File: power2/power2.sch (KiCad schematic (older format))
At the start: 40 parts, among them P1 CN3 from HL, P2 CONN_01X02, P3 CONN_01X03, P4 CONN_02X06, P5 CONN_01X02, P6 CONN_01X08, U1 ADC78H90CIMT, U2 Oki 5V Reg, U3 Oki 3.3V Reg, U4 LMC6482A

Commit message: v2rx changes and update to new kicad
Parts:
- C1: symbol CP1 -> CP1-RESCUE-power2
- C10, C11, C2, C3, C4, C9: symbol C -> C-RESCUE-power2
- D1, D2: footprint Diodes_SMD:SOD-123 -> (none)
- D3: value BZX84C 3V3 -> BZXB4C 3v3; footprint Diodes_SMD:SOD-123 -> (none)
- R1, R10, R2, R3, R4, R5, R6, R7, R8, R9: symbol R -> R-RESCUE-power2
- U4: symbol OP275 -> OP275-RESCUE-power2
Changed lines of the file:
@@
 EESchema Schematic File Version 2
+LIBS:power2-rescue
 LIBS:power
 LIBS:device
@@
 LIBS:memory
 LIBS:xilinx
-LIBS:special
 LIBS:microcontrollers
 LIBS:dsp
@@
 	4650 1100 5150 1100
 $Comp
-L GND #PWR01
+L GND-RESCUE-power2 #PWR01
 U 1 1 54BE578A
 P 6250 1500
@@
 $EndComp
 $Comp
-L GND #PWR02
+L GND-RESCUE-power2 #PWR02
 U 1 1 54B9B387
 P 5150 1500
@@
 	4650 1200 4750 1200
 $Comp
-L GND #PWR03
+L GND-RESCUE-power2 #PWR03
 U 1 1 54B935E9
 P 4750 1500
@@
 $EndComp
 $Comp
-L CP1 C1
+L CP1-RESCUE-power2 C1
 U 1 1 54B82D65
 P 5150 1300
@@
 $EndComp
 $Comp
-L C C2
+L C-RESCUE-power2 C2
 U 1 1 551AAA77
 P 6250 1300
@@
 	10300 1100 10300 1800
 $Comp
-L GND #PWR04
+L GND-RESCUE-power2 #PWR04
 U 1 1 551AB7A4
 P 10300 1800
@@
 Connection ~ 10300 1200
 $Comp
-L GND #PWR05
+L GND-RESCUE-power2 #PWR05
 U 1 1 551ABA3D
 P 6900 1400
@@
 $EndComp
 $Comp
-L GND #PWR06
+L GND-RESCUE-power2 #PWR06
 U 1 1 551ABA65
 P 7800 1900
@@
 	8600 1600 8800 1600
 $Comp
-L GND #PWR07
+L GND-RESCUE-power2 #PWR07
 U 1 1 551AC024
 P 8450 1700
@@
 $EndComp
 $Comp
-L GND #PWR08
+L GND-RESCUE-power2 #PWR08
 U 1 1 551AC04B
 P 8500 1200
@@
 	9500 2600 9500 2750
 $Comp
-L GND #PWR09
+L GND-RESCUE-power2 #PWR09
 U 1 1 551AC911
 P 9500 2750
@@
 	9000 2500 9600 2500
 $Comp
-L GND #PWR010
+L GND-RESCUE-power2 #PWR010
 U 1 1 551ACBE1
 P 7950 2500
@@
 $EndComp
 $Comp
-L GND #PWR011
+L GND-RESCUE-power2 #PWR011
 U 1 1 551ACBFA
 P 8450 2800
@@
 	7600 3000 7600 3500
 $Comp
-L GND #PWR012
+L GND-RESCUE-power2 #PWR012
 U 1 1 551ACC6B
 P 7600 3500
@@
 	7200 3750 6350 3750
 $Comp
-L C C4
+L C-RESCUE-power2 C4
 U 1 1 551ACF21
 P 7000 3950
@@
 $EndComp
 $Comp
-L C C3
+L C-RESCUE-power2 C3
 U 1 1 551ACFBF
 P 6600 3950
@@
 $EndComp
 $Comp
-L GND #PWR013
+L GND-RESCUE-power2 #PWR013
 U 1 1 551AD095
 P 7000 4150
@@
 $EndComp
 $Comp
-L GND #PWR014
+L GND-RESCUE-power2 #PWR014
 U 1 1 551AD0B1
 P 6600 4150
@@
 	6000 3300 6000 3500
 $Comp
-L GND #PWR015
+L GND-RESCUE-power2 #PWR015
 U 1 1 551AD402
 P 6000 3500
@@
 Connection ~ 7600 3500
 $Comp
-L OP275 U4
+L OP275-RESCUE-power2 U4
 U 1 1 552BFD56
 P 6600 5000
@@
 $EndComp
 $Comp
-L OP275 U4
+L OP275-RESCUE-power2 U4
 U 2 1 552BFF04
 P 8100 5100
@@
 $EndComp
 $Comp
-L R R7
+L R-RESCUE-power2 R7
 U 1 1 552C03C4
 P 7800 5950
@@
 $EndComp
 $Comp
-L R R5
+L R-RESCUE-power2 R5
 U 1 1 552C077F
 P 7300 5000
@@
 $EndComp
 $Comp
-L R R6
+L R-RESCUE-power2 R6
 U 1 1 552C08A2
 P 7550 5450
@@
 $EndComp
 $Comp
-L R R8
+L R-RESCUE-power2 R8
 U 1 1 552C0983
 P 8450 5950
@@
 $EndComp
 $Comp
-L R R4
+L R-RESCUE-power2 R4
 U 1 1 552C09E6
 P 6200 5950
@@
 $EndComp
 $Comp
-L R R3
+L R-RESCUE-power2 R3
 U 1 1 552C0A88
 P 5900 5450
@@
 	5900 4900 5900 5200
 $Comp
-L GND #PWR016
+L GND-RESCUE-power2 #PWR016
 U 1 1 552C11D9
 P 6500 5300
@@
 	1    0    0    -1
 $EndComp
-$Comp
-L ZENER D2
-U 1 1 552C183F
-P 6650 5950
-F 0 "D2" H 6650 6050 50  0000 C CNN
-F 1 "1n5711" H 6650 5850 40  0000 C CNN
-F 2 "Diodes_SMD:SOD-123" H 6650 5950 60  0001 C CNN
-F 3 "" H 6650 5950 60  0000 C CNN
-	1    6650 5950
-	-1   0    0    1
-$EndComp
 Wire Wire Line
 	6950 5000 6950 5950
@@
 	6950 5950 6850 5950
 $Comp
-L GND #PWR017
+L GND-RESCUE-power2 #PWR017
 U 1 1 552C18EE
 P 5900 6050
@@
 $EndComp
 $Comp
-L GND #PWR018
+L GND-RESCUE-power2 #PWR018
 U 1 1 552C1913
 P 7550 6050
@@
 Connection ~ 5900 4900
 $Comp
-L R R2
+L R-RESCUE-power2 R2
 U 1 1 552C3533
 P 5500 5150
@@
 $EndComp
 $Comp
-L R R1
+L R-RESCUE-power2 R1
 U 1 1 552C36C8
 P 5500 4650
@@
 $EndComp
 $Comp
-L GND #PWR019
+L GND-RESCUE-power2 #PWR019
 U 1 1 552C39B6
 P 5500 5400
@@
 $EndComp
 $Comp
-L GND #PWR020
+L GND-RESCUE-power2 #PWR020
 U 1 1 552C3A08
 P 4650 4600
@@
 F 3 "" H 4650 4600 50  0000 C CNN
 	1    4650 4600
-	1    0    0    -1
-$EndComp
-$Comp
-L ZENER D1
-U 1 1 552C3BD5
-P 5700 4900
-F 0 "D1" H 5700 5000 50  0000 C CNN
-F 1 "1n5711" H 5700 4800 40  0000 C CNN
-F 2 "Diodes_SMD:SOD-123" H 5700 4900 60  0001 C CNN
-F 3 "" H 5700 4900 60  0000 C CNN
-	1    5700 4900
 	1    0    0    -1
 $EndComp
@@
 	4650 4500 4650 4600
 $Comp
-L C C9
+L C-RESCUE-power2 C9
 U 1 1 5530FFE1
 P 6100 5450
@@
 nADCCS
 $Comp
-L C C10
+L C-RESCUE-power2 C10
 U 1 1 5554C716
 P 5000 4400
@@
 Wire Wire Line
 	5200 4400 5500 4400
-$Comp
-L ZENER D3
-U 1 1 5558A709
-P 9000 3650
-F 0 "D3" H 9000 3750 50  0000 C CNN
-F 1 "BZX84C 3V3" H 9000 3550 40  0000 C CNN
-F 2 "Diodes_SMD:SOD-123" H 9000 3650 60  0001 C CNN
-F 3 "" H 9000 3650 60  0000 C CNN
-	1    9000 3650
-	0    -1   -1   0
-$EndComp
 Wire Wire Line
 	7850 2800 7850 4600
@@
 	8800 5100 8800 5950
 $Comp
-L R R10
+L R-RESCUE-power2 R10
 U 1 1 5558AFB4
 P 8700 3700
@@
 $EndComp
 $Comp
-L C C11
+L C-RESCUE-power2 C11
 U 1 1 5558B07B
 P 8400 3650
@@
 Connection ~ 6500 1600
 $Comp
-L R R9
+L R-RESCUE-power2 R9
 U 1 1 5558B562
 P 8700 3200
@@
 	8700 3950 8700 4050
 $Comp
-L GND #PWR021
+L GND-RESCUE-power2 #PWR021
 U 1 1 5558BF22
 P 8700 4050
@@
 	1300 2250 1300 2300
 $Comp
-L GND #PWR022
+L GND-RESCUE-power2 #PWR022
 U 1 1 558C247A
 P 1300 2300
@@
 $EndComp
 $Comp
-L GND #PWR023
+L GND-RESCUE-power2 #PWR023
 U 1 1 558FEEE6
 P 1850 2600
@@
 $EndComp
 $Comp
-L GND #PWR024
+L GND-RESCUE-power2 #PWR024
 U 1 1 558FEF19
 P 2450 2900
@@
 $EndComp
 $Comp
-L GND #PWR025
+L GND-RESCUE-power2 #PWR025
 U 1 1 558FEF4C
 P 2450 3300
@@
 $EndComp
 $Comp
-L GND #PWR026
+L GND-RESCUE-power2 #PWR026
 U 1 1 558FF17C
 P 1850 3000
@@
 Wire Wire Line
 	4700 2900 4600 2900
+$Comp
+L ZENER D1
+U 1 1 5675BF74
+P 5700 4900
+F 0 "D1" H 5700 5000 50  0000 C CNN
+F 1 "1n5711" H 5700 4800 50  0000 C CNN
+F 2 "" H 5700 4900 50  0001 C CNN
+F 3 "" H 5700 4900 50  0000 C CNN
+	1    5700 4900
+	-1   0    0    1
+$EndComp
+$Comp
+L ZENER D2
+U 1 1 5675C3B1
+P 6650 5950
+F 0 "D2" H 6650 6050 50  0000 C CNN
+F 1 "1n5711" H 6650 5850 50  0000 C CNN
+F 2 "" H 6650 5950 50  0001 C CNN
+F 3 "" H 6650 5950 50  0000 C CNN
+	1    6650 5950
+	1    0    0    -1
+$EndComp
+$Comp
+L ZENER D3
+U 1 1 5675DDD3
+P 9000 3650
+F 0 "D3" H 9000 3750 50  0000 C CNN
+F 1 "BZXB4C 3v3" H 9050 3550 50  0000 C CNN
+F 2 "" H 9000 3650 50  0001 C CNN
+F 3 "" H 9000 3650 50  0000 C CNN
+	1    9000 3650
+	0    1    1    0
+$EndComp
 $EndSCHEMATC

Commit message: Latest Rx updates
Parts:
- removed C12, C13, C14, C15: NFM21PC224R1C3D, SMDCAP:cfeed_0805, symbol Cap_FeedThrough
- removed P6: CONN_01X08, Pin_Headers:Pin_Header_Straight_1x08, symbol CONN_01X08
- added P6: CONN_01X05, symbol CONN_01X05
- added R11: 1k, Resistors_SMD:R_0805_HandSoldering, symbol R-RESCUE-power2
- added R12: 270, Resistors_SMD:R_0805_HandSoldering, symbol R-RESCUE-power2
- added R13, R14: 10k, Resistors_SMD:R_0805_HandSoldering, symbol R-RESCUE-power2
- added U5: LTV-847, DIP-16, symbol LTV-847
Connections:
- net GND: now also P6.1 (P1), P6.5 (P5), U5.11, U5.13, U5.15, U5.4, U5.9
- net at C2.1, L1.2, R9.1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: now also R11.1
- net at C6.2, L2.1, P4.5 (P5)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: now also R13.1, R14.1
- net at P1.10 (P10): now also R13.2, U5.16
- net at P1.6 (P6): now also R14.2, U5.12
- net at P1.8 (P8): now also R12.1
- new net: R11.2, U5.1, U5.5
- new net: R12.2, U5.3
- new net: P6.3 (P3), U5.14
- new net: P6.2 (P2), U5.2
- new net: P6.4 (P4), U5.6
- no-connect marks 3 -> 10
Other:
- note added: "CW in"
- note added: "CW out"
- note added: "P39 CN1 (3)"
- note added: "P41 CN1 (5)"
- note added: "P45 CN1 (7)"
- note added: "PTT in"
- note removed: "P39 CN1"
- note removed: "P41 CN1"
- note removed: "P45 CN1"

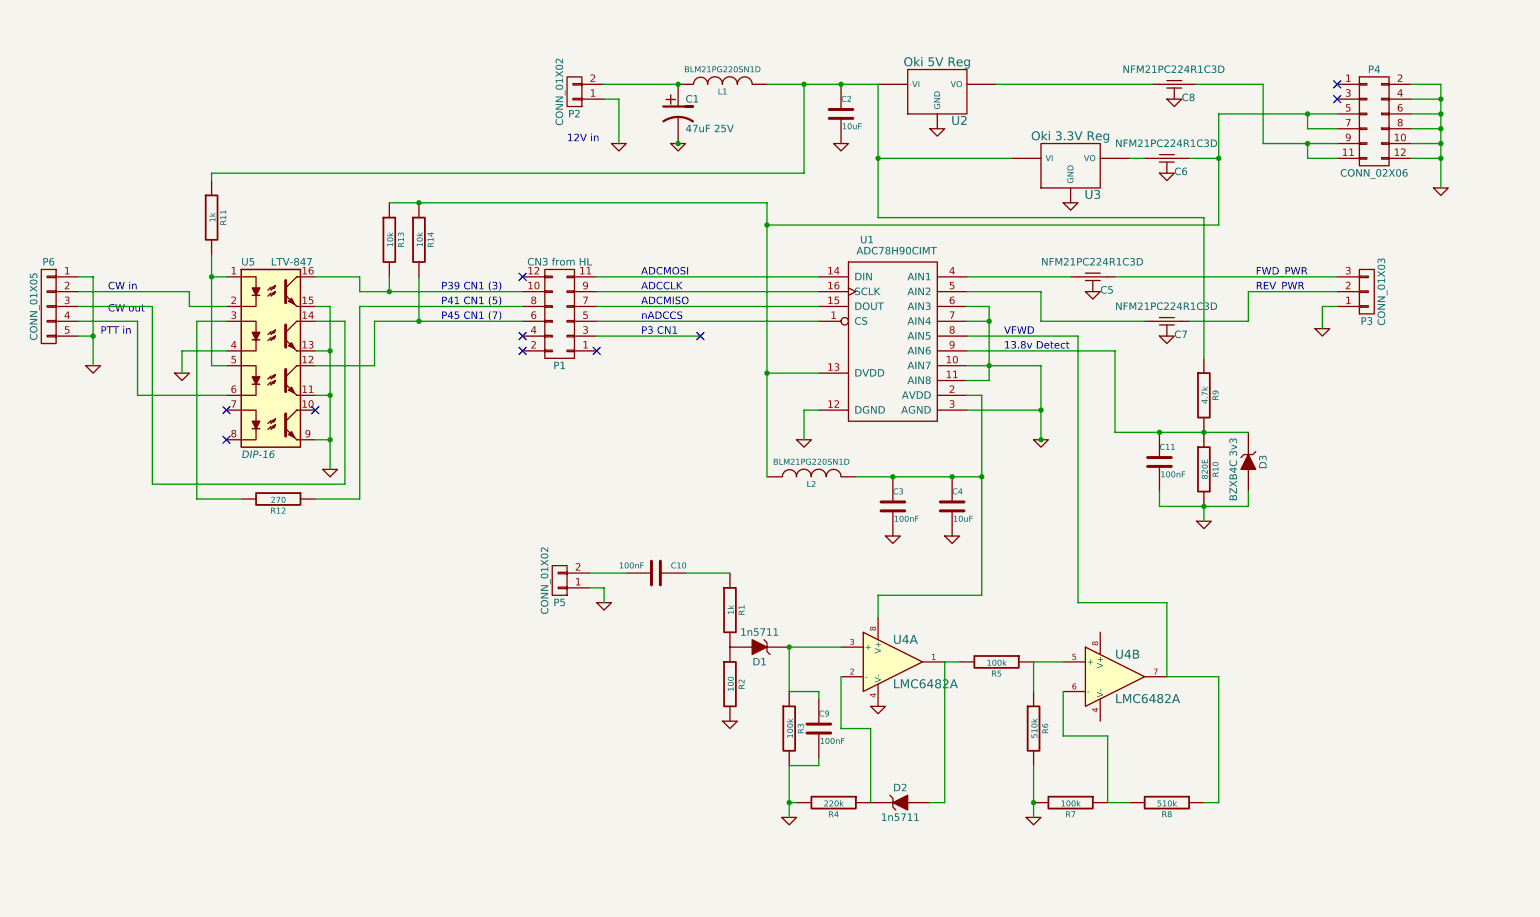
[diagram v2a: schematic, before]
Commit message: Updates for v1.1 amp and V1.4 ADC
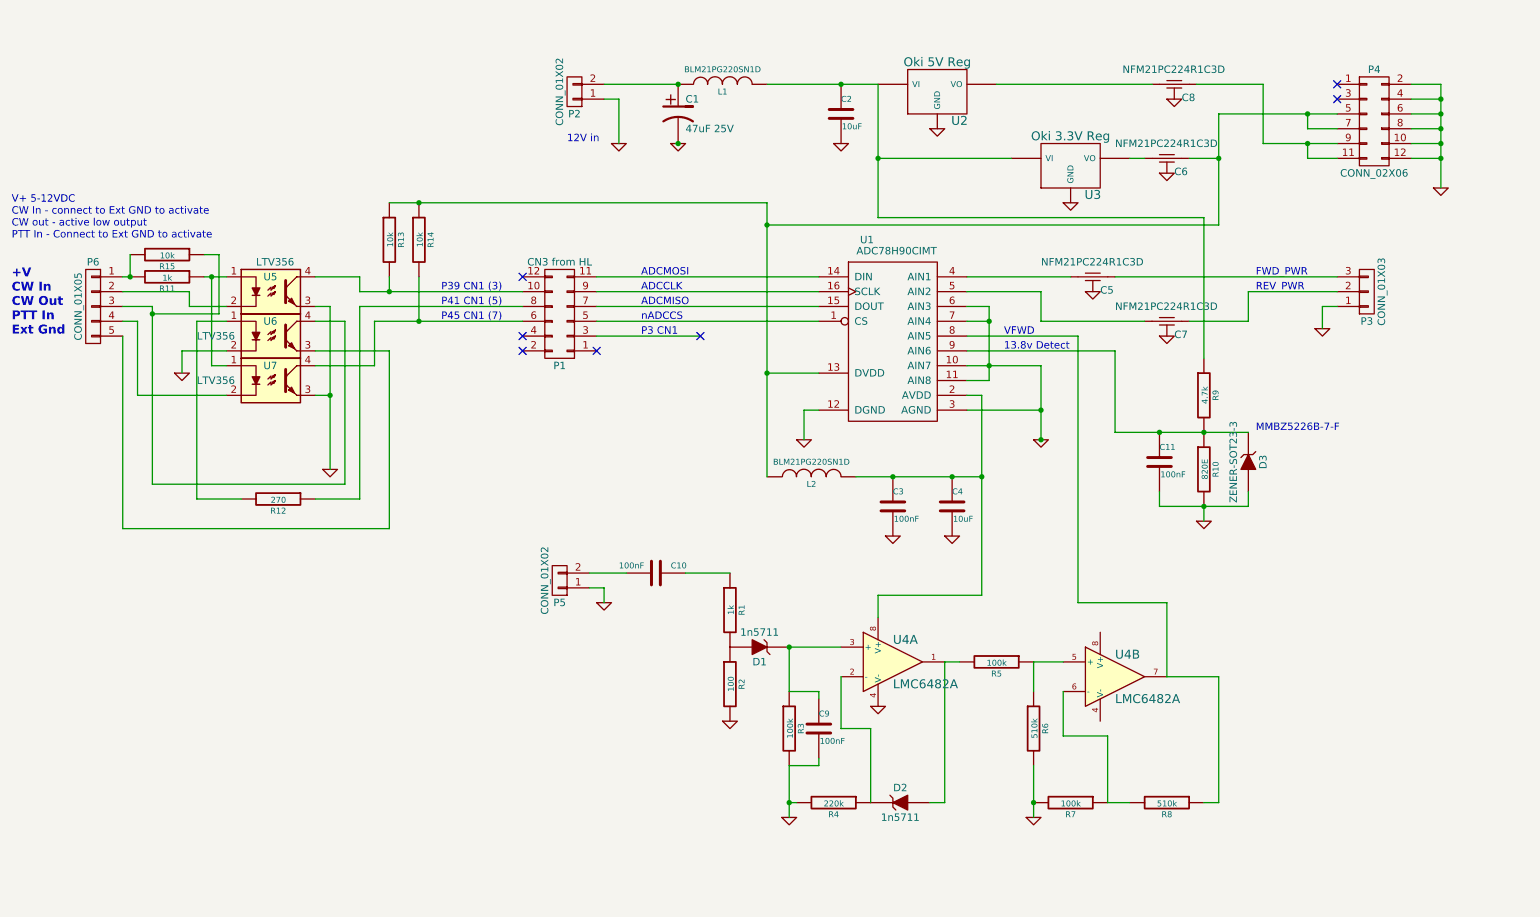
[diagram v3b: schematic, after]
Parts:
- removed D3: BZXB4C 3v3, symbol ZENER
- removed U5: LTV-847, DIP-16, symbol LTV-847
- added D3: ZENER-SOT23-3, symbol ZENER-SOT23-3
- added R15: 10k, Resistors_SMD:R_0805_HandSoldering, symbol R-RESCUE-power2
- added U5, U6, U7: LTV356, Opto-Devices:Optocoupler_SMD_HandSoldering_KPC357_LTV35x_PC357_SingleChannel, symbol PC817
- D1, D2: footprint (none) -> Diodes_SMD:SOD-123
- P6: footprint (none) -> Pin_Headers:Pin_Header_Straight_1x05
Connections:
- net GND: now also D3.2 (A), U5.3, U6.2, U7.3; no longer P6.1 (P1), P6.5 (P5)
- net at C2.1, L1.2, R9.1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: no longer R11.1
- net at P1.10 (P10), R13.2: now also U5.4
- net at P1.6 (P6), R14.2: now also U7.4
- net at C11.1, R10.1, R9.2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: now also D3.3 (K)
- net at R11.2: now also P6.1 (P1), R15.2
- net at R12.2: now also U6.1
- net at P6.3 (P3): now also R15.1, U6.4
- net at P6.2 (P2): now also U5.2
- net at P6.4 (P4): now also U7.2
- new net: R11.1, U5.1, U7.1
- new net: P6.5 (P5), U6.3
- no-connect marks 10 -> 7
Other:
- note added: "+V\nCW In\nCW Out\nPTT In\nExt Gnd"
- note added: "MMBZ5226B-7-F"
- note added: "V+ 5-12VDC\nCW In - connect to Ext GND to activate\nCW out - active low output\nPTT In - Connect to Ext GND to activate"
- note removed: "CW in"
- note removed: "CW out"
- note removed: "PTT in"
- moved on the sheet: P6, R11
